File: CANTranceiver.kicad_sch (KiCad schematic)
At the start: 1 part, among them U3 IC TRANSCEIVER 1/1 8SO

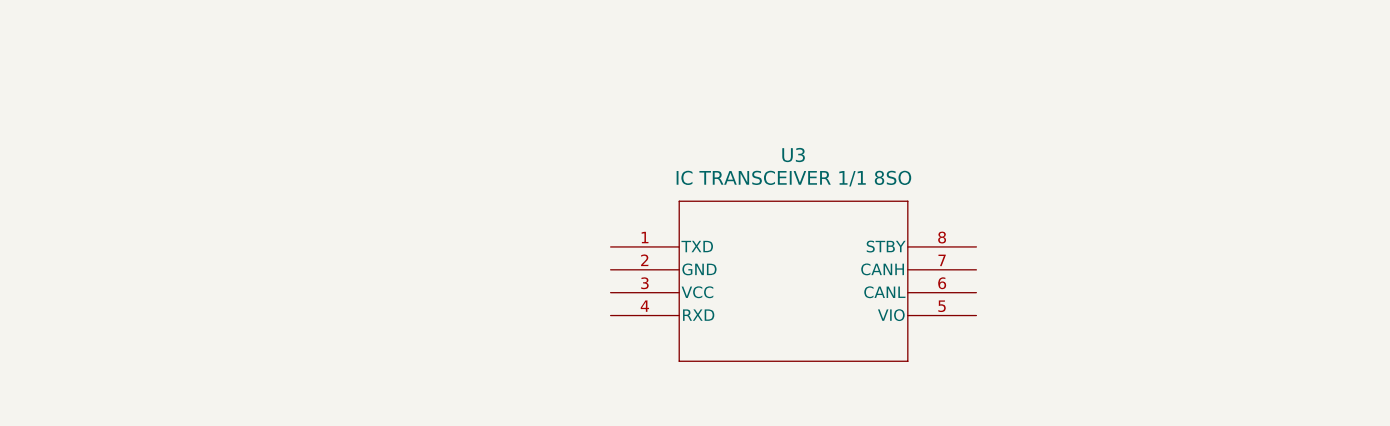
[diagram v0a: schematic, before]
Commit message: added stm pins
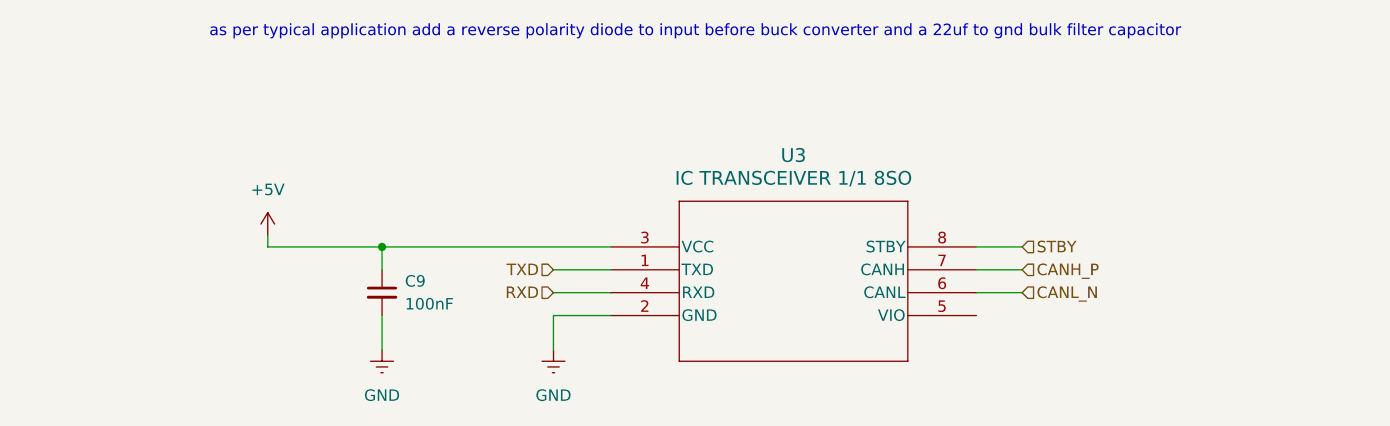
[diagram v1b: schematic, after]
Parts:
- added C9: 100nF, symbol Device:C_Small
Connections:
- net TXD: now reaches U3.1 (TXD)
- net GND: now reaches U3.2 (GND)
- net GND: now also C9.2
- net +5V: now reaches U3.3 (VCC)
- net +5V: now also C9.1
- net RXD: now reaches U3.4 (RXD)
- net CANL_N: now reaches U3.6 (CANL)
- net CANH_P: now reaches U3.7 (CANH)
- net STBY: now reaches U3.8 (STBY)
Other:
- note added: "as per typical application add a reverse polarity diode to input before buck converter and a 22uf to gnd bulk filter capacitor"

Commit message: finished can and power
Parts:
- added C11: 100nF, symbol Device:C_Small
- added C12: 22uF, symbol Device:C_Small_US
- added C13: 4.7nF, symbol Device:C_Small
- added D2: DIODE SCHOTTKY 30V 1A SOD323F, footprints:P39_SOD-323P, symbol symbols:SDB13HS-AQ
- added R10, R11: 60, symbol Device:R_Small_US
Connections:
- net CANH_P: now also R10.1, R11.2
- net GND: now also C11.2, C12.2, C13.2
- net 3V3: now reaches U3.5 (VIO)
- net 3V3: now also C11.1
- net +5V: no longer names the net of C9.1, U3.3 (VCC)
- net +5V: now also C12.1, D2.1 (K)
- net CANL_N renamed CANL_Filt
- new net: C13.1, R10.2, R11.1
- new net 5V: D2.2 (A)
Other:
- note added: "CANBus Split Termination"
- note removed: "as per typical application add a reverse polarity diode to input before buck converter and a 22uf to gnd bulk filter capacitor"
- moved on the sheet: C9, U3

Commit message: schematic done
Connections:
- net CANH_P: no longer R11.2
- net CANL_Filt renamed CANL_N
- net CANL_N: now also R11.2
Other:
- moved on the sheet: C11
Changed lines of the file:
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@@
-	)
-	(junction
-		(at 153.67 130.81)
-		(diameter 0)
-		(color 0 0 0 0)
 	)
 	(junction
@@
 	)
 	(junction
-		(at 153.67 97.79)
+		(at 106.68 60.96)
 		(diameter 0)
 		(color 0 0 0 0)
 	)
 	(junction
-		(at 106.68 60.96)
+		(at 195.58 68.58)
 		(diameter 0)
 		(color 0 0 0 0)
@@
 		(color 0 0 0 0)
 	)
-	(junction
-		(at 203.2 68.58)
-		(diameter 0)
-		(color 0 0 0 0)
-	)
-	(wire
-		(pts
-			(xy 203.2 76.2) (xy 203.2 78.74)
+	(wire
+		(pts
+			(xy 195.58 76.2) (xy 195.58 78.74)
 		)
 		(stroke
@@
 	(wire
 		(pts
+			(xy 195.58 68.58) (xy 195.58 71.12)
+		)
+		(stroke
+			(width 0)
+			(type default)
+		)
+	)
+	(wire
+		(pts
 			(xy 165.1 111.76) (xy 165.1 114.3)
 		)
@@
 	(wire
 		(pts
-			(xy 203.2 71.12) (xy 203.2 68.58)
-		)
-		(stroke
-			(width 0)
-			(type default)
-		)
-	)
-	(wire
-		(pts
-			(xy 203.2 68.58) (xy 172.72 68.58)
+			(xy 195.58 66.04) (xy 195.58 68.58)
 		)
 		(stroke
@@
 	(wire
 		(pts
-			(xy 172.72 63.5) (xy 186.69 63.5)
+			(xy 172.72 63.5) (xy 177.8 63.5)
 		)
 		(stroke
@@
 	(wire
 		(pts
-			(xy 153.67 130.81) (xy 162.56 130.81)
-		)
-		(stroke
-			(width 0)
-			(type default)
-		)
-	)
-	(wire
-		(pts
-			(xy 153.67 97.79) (xy 166.37 97.79)
-		)
-		(stroke
-			(width 0)
-			(type default)
-		)
-	)
-	(wire
-		(pts
 			(xy 172.72 60.96) (xy 177.8 60.96)
 		)
@@
 	(wire
 		(pts
-			(xy 203.2 66.04) (xy 203.2 68.58)
-		)
-		(stroke
-			(width 0)
-			(type default)
-		)
-	)
-	(wire
-		(pts
 			(xy 90.17 60.96) (xy 106.68 60.96)
 		)
@@
 	(wire
 		(pts
-			(xy 172.72 66.04) (xy 186.69 66.04)
+			(xy 172.72 66.04) (xy 177.8 66.04)
 		)
 		(stroke
@@
 	(wire
 		(pts
+			(xy 172.72 68.58) (xy 195.58 68.58)
+		)
+		(stroke
+			(width 0)
+			(type default)
+		)
+	)
+	(wire
+		(pts
 			(xy 153.67 121.92) (xy 153.67 130.81)
 		)
@@
 			(width 0)
 			(type default)
-		)
-	)
-	(label "CANH_Filt"
-		(at 143.51 130.81 180)
-		(effects
-			(font
-				(size 1.27 1.27)
-			)
-			(justify right bottom)
-		)
-	)
-	(label "CANH_Filt"
-		(at 143.51 97.79 180)
-		(effects
-			(font
-				(size 1.27 1.27)
-			)
-			(justify right bottom)
-		)
-	)
-	(label "CANL_Filt"
-		(at 186.69 66.04 0)
-		(effects
-			(font
-				(size 1.27 1.27)
-			)
-			(justify left bottom)
-		)
-	)
-	(label "CANH_Filt"
-		(at 186.69 63.5 0)
-		(effects
-			(font
-				(size 1.27 1.27)
-			)
-			(justify left bottom)
 		)
 	)
@@
 		)
 	)
+	(hierarchical_label "CANH_P"
+		(shape input)
+		(at 143.51 97.79 180)
+		(effects
+			(font
+				(size 1.27 1.27)
+			)
+			(justify right)
+		)
+	)
 	(hierarchical_label "CANL_N"
 		(shape input)
-		(at 162.56 130.81 0)
+		(at 177.8 66.04 0)
+		(effects
+			(font
+				(size 1.27 1.27)
+			)
+			(justify left)
+		)
+	)
+	(hierarchical_label "CANH_P"
+		(shape input)
+		(at 177.8 63.5 0)
 		(effects
 			(font
@@
 		)
 	)
-	(hierarchical_label "CANH_P"
+	(hierarchical_label "CANL_N"
 		(shape input)
-		(at 166.37 97.79 0)
+		(at 143.51 130.81 180)
 		(effects
 			(font
 				(size 1.27 1.27)
 			)
-			(justify left)
+			(justify right)
 		)
 	)
@@
 	(symbol
 		(lib_id "power:GNDREF")
-		(at 203.2 78.74 0)
+		(at 195.58 78.74 0)
 		(unit 1)
 		(body_style 1)
@@
 		(fields_autoplaced yes)
 		(property "Reference" "#PWR026"
-			(at 203.2 85.09 0)
+			(at 195.58 85.09 0)
 			(hide yes)
 			(show_name no)
@@
 		)
 		(property "Value" "GND"
-			(at 203.2 83.82 0)
+			(at 195.58 83.82 0)
 			(show_name no)
 			(do_not_autoplace no)
@@
 		)
 		(property "Footprint" ""
-			(at 203.2 78.74 0)
+			(at 195.58 78.74 0)
 			(hide yes)
 			(show_name no)
@@
 		)
 		(property "Datasheet" ""
-			(at 203.2 78.74 0)
+			(at 195.58 78.74 0)
 			(hide yes)
 			(show_name no)
@@
 		)
 		(property "Description" "Power symbol creates a global label with name \"GNDREF\" , reference supply ground"
-			(at 203.2 78.74 0)
+			(at 195.58 78.74 0)
 			(hide yes)
 			(show_name no)
@@
 	(symbol
 		(lib_id "Device:C_Small")
-		(at 203.2 73.66 0)
+		(at 195.58 73.66 0)
 		(unit 1)
 		(body_style 1)
@@
 		(fields_autoplaced yes)
 		(property "Reference" "C11"
-			(at 205.74 72.3962 0)
+			(at 198.12 72.3962 0)
 			(show_name no)
 			(do_not_autoplace no)
@@
 		)
 		(property "Value" "100nF"
-			(at 205.74 74.9362 0)
+			(at 198.12 74.9362 0)
 			(show_name no)
 			(do_not_autoplace no)
@@
 		)
 		(property "Footprint" ""
-			(at 203.2 73.66 0)
+			(at 195.58 73.66 0)
 			(hide yes)
 			(show_name no)
@@
 		)
 		(property "Datasheet" ""
-			(at 203.2 73.66 0)
+			(at 195.58 73.66 0)
 			(hide yes)
 			(show_name no)
@@
 		)
 		(property "Description" "Unpolarized capacitor, small symbol"
-			(at 203.2 73.66 0)
+			(at 195.58 73.66 0)
 			(hide yes)
 			(show_name no)
@@
 	(symbol
 		(lib_id "power:+5V")
-		(at 203.2 66.04 0)
+		(at 195.58 66.04 0)
 		(unit 1)
 		(body_style 1)
@@
 		(fields_autoplaced yes)
 		(property "Reference" "#PWR027"
-			(at 203.2 69.85 0)
+			(at 195.58 69.85 0)
 			(hide yes)
 			(show_name no)
@@
 		)
 		(property "Value" "3V3"
-			(at 203.2 60.96 0)
+			(at 195.58 60.96 0)
 			(show_name no)
 			(do_not_autoplace no)
@@
 		)
 		(property "Footprint" ""
-			(at 203.2 66.04 0)
+			(at 195.58 66.04 0)
 			(hide yes)
 			(show_name no)
@@
 		)
 		(property "Datasheet" ""
-			(at 203.2 66.04 0)
+			(at 195.58 66.04 0)
 			(hide yes)
 			(show_name no)
@@
 		)
 		(property "Description" "Power symbol creates a global label with name \"+5V\""
-			(at 203.2 66.04 0)
-			(hide yes)
-			(show_name no)
+			(at 195.58 66.04 0)
+			(hide yes)
+			(show_name no)

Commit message: damir review
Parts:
- removed D2: DIODE SCHOTTKY 30V 1A SOD323F, footprints:P39_SOD-323P, symbol symbols:SDB13HS-AQ
- added D1, D2: TVS DIODE 36VWM 76.8VC SOT233, footprints:P200_SOT-23, symbol symbols:Diode-NC_pin
- R10, R11: value 60 -> 60.4
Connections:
- net 5V: now also C12.1, C9.1, U3.3 (VCC)
- net CANH_P: now also D1.2 (C)
- net CANL_N: now also D2.2 (C)
- net GND: now also D1.1 (A), D2.1 (A)
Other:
- note added: "C = 1/2piRf = 5.3nF -> 4.7nF f = 500kHz R = 60.4"

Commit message: tweaked a little
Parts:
- removed D1, D2: TVS DIODE 36VWM 76.8VC SOT233, footprints:P200_SOT-23, symbol symbols:Diode-NC_pin
- added D4, D5: TVS DIODE 5VWM 12.5VC SOD-523, footprints:P38_SOD-523, symbol symbols:Diode
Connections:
- net CANH_P: now also D4.2 (C)
- net CANL_N: now also D5.2 (C)
- net GND: now also D4.1 (A), D5.1 (A)
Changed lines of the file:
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@@
+	)
+	(symbol
+		(lib_id "symbols:Diode")
+		(at 137.16 104.14 90)
+		(unit 1)
+		(body_style 1)
+		(exclude_from_sim no)
+		(in_bom yes)
+		(on_board yes)
+		(in_pos_files yes)
+		(dnp no)
+		(property "Reference" "D4"
+			(at 130.302 102.87 90)
+			(show_name no)
+			(do_not_autoplace no)
+			(effects
+				(font
+					(size 1.27 1.27)
+				)
+				(justify right)
+			)
+		)
+		(property "Value" "TVS DIODE 5VWM 12.5VC SOD-523"
+			(at 99.314 105.156 90)
+			(show_name no)
+			(do_not_autoplace no)
+			(effects
+				(font
+					(size 1.27 1.27)
+				)
+				(justify right)
+			)
+		)
+		(property "Footprint" "footprints:P38_SOD-523"
+			(at 135.89 104.14 90)
+			(hide yes)
+			(show_name no)
+			(do_not_autoplace no)
+			(effects
+				(font
+					(size 1.27 1.27)
+				)
+			)
+		)
+		(property "Datasheet" "https://www.digikey.ca/en/products/detail/diotec-semiconductor/ESD5B5V0WT/22189401"
+			(at 139.7 104.14 0)
+			(hide yes)
+			(show_name no)
+			(do_not_autoplace no)
+			(effects
+				(font
+					(size 1.27 1.27)
+				)
+			)
+		)
+		(property "Description" "12.5V Clamp 4A (8/20µs) Ipp Tvs Diode Surface Mount SOD-523"
+			(at 137.16 104.14 0)
+			(hide yes)
+			(show_name no)
+			(do_not_autoplace no)
+			(effects
+				(font
+					(size 1.27 1.27)
+				)
+			)
+		)
+		(pin "2"
+		)
+		(pin "1"
+		)
+		(instances
+			(project "bms-main"
+				(path "/d7e1c873-142c-4805-8303-47f5b9830fe8/3499863e-1965-40fb-acb8-8c0f2bec52b8"
+					(reference "D4")
+					(unit 1)
+				)
+			)
+		)
 	)
 	(symbol
@@
 	)
 	(symbol
-		(lib_id "symbols:Diode-NC_pin")
-		(at 140.97 137.16 90)
-		(unit 1)
-		(body_style 1)
-		(exclude_from_sim no)
-		(in_bom yes)
-		(on_board yes)
-		(in_pos_files yes)
-		(dnp no)
-		(fields_autoplaced yes)
-		(property "Reference" "D2"
-			(at 144.78 135.9534 90)
-			(show_name no)
-			(do_not_autoplace no)
-			(effects
-				(font
-					(size 1.27 1.27)
-				)
-				(justify right)
-			)
-		)
-		(property "Value" "TVS DIODE 36VWM 76.8VC SOT233"
-			(at 144.78 138.4934 90)
-			(show_name no)
-			(do_not_autoplace no)
-			(effects
-				(font
-					(size 1.27 1.27)
-				)
-				(justify right)
-			)
-		)
-		(property "Footprint" "footprints:P200_SOT-23"
-			(at 137.16 138.43 90)
-			(hide yes)
-			(show_name no)
-			(do_not_autoplace no)
-			(effects
-				(font
-					(size 1.27 1.27)
-				)
-			)
-		)
-		(property "Datasheet" "https://www.digikey.ca/en/products/detail/diotec-semiconductor/PSOT36C/22191308"
-			(at 146.05 137.16 0)
-			(hide yes)
-			(show_name no)
-			(do_not_autoplace no)
-			(effects
-				(font
-					(size 1.27 1.27)
-				)
-			)
-		)
-		(property "Description" "76.8V Clamp 9A (8/20µs) Ipp Tvs Diode Surface Mount SOT-23-3 (TO-236)"
-			(at 140.97 137.16 0)
-			(hide yes)
-			(show_name no)
-			(do_not_autoplace no)
-			(effects
-				(font
-					(size 1.27 1.27)
-				)
-			)
-		)
-		(pin "1"
-		)
-		(pin "3"
-		)
-		(pin "2"
-		)
-		(instances
-			(project "bms-main"
-				(path "/d7e1c873-142c-4805-8303-47f5b9830fe8/3499863e-1965-40fb-acb8-8c0f2bec52b8"
-					(reference "D2")
-					(unit 1)
-				)
-			)
-		)
-	)
-	(symbol
 		(lib_id "power:GNDREF")
 		(at 90.17 73.66 0)
@@
 	)
 	(symbol
-		(lib_id "symbols:Diode-NC_pin")
-		(at 139.7 102.87 90)
-		(unit 1)
-		(body_style 1)
-		(exclude_from_sim no)
-		(in_bom yes)
-		(on_board yes)
-		(in_pos_files yes)
-		(dnp no)
-		(property "Reference" "D1"
-			(at 100.584 102.616 90)
-			(show_name no)
-			(do_not_autoplace no)
-			(effects
-				(font
-					(size 1.27 1.27)
-				)
-				(justify right)
-			)
-		)
-		(property "Value" "TVS DIODE 36VWM 76.8VC SOT233"
-			(at 100.584 105.156 90)
-			(show_name no)
-			(do_not_autoplace no)
-			(effects
-				(font
-					(size 1.27 1.27)
-				)
-				(justify right)
-			)
-		)
-		(property "Footprint" "footprints:P200_SOT-23"
-			(at 135.89 104.14 90)
-			(hide yes)
-			(show_name no)
-			(do_not_autoplace no)
-			(effects
-				(font
-					(size 1.27 1.27)
-				)
-			)
-		)
-		(property "Datasheet" "https://www.digikey.ca/en/products/detail/diotec-semiconductor/PSOT36C/22191308"
-			(at 144.78 102.87 0)
-			(hide yes)
-			(show_name no)
-			(do_not_autoplace no)
-			(effects
-				(font
-					(size 1.27 1.27)
-				)
-			)
-		)
-		(property "Description" "76.8V Clamp 9A (8/20µs) Ipp Tvs Diode Surface Mount SOT-23-3 (TO-236)"
-			(at 139.7 102.87 0)
-			(hide yes)
-			(show_name no)
-			(do_not_autoplace no)
-			(effects
-				(font
-					(size 1.27 1.27)
-				)
-			)
-		)
-		(pin "1"
-		)
-		(pin "3"
-		)
-		(pin "2"
-		)
-		(instances
-			(project "bms-main"
-				(path "/d7e1c873-142c-4805-8303-47f5b9830fe8/3499863e-1965-40fb-acb8-8c0f2bec52b8"
-					(reference "D1")
-					(unit 1)
-				)
-			)
-		)
-	)
-	(symbol
 		(lib_id "Device:R_Small_US")
 		(at 153.67 106.68 0)
@@
 					(unit 1)
 				)
+			)
+		)
+	)
+	(symbol
+		(lib_id "symbols:Diode")
+		(at 138.43 138.43 90)
+		(unit 1)
+		(body_style 1)
+		(exclude_from_sim no)
+		(in_bom yes)
+		(on_board yes)
+		(in_pos_files yes)
+		(dnp no)
+		(fields_autoplaced yes)
+		(property "Reference" "D5"
+			(at 140.97 137.1599 90)
+			(show_name no)
+			(do_not_autoplace no)
+			(effects
+				(font
+					(size 1.27 1.27)
+				)
+				(justify right)
+			)
+		)
+		(property "Value" "TVS DIODE 5VWM 12.5VC SOD-523"
+			(at 140.97 139.6999 90)
+			(show_name no)
+			(do_not_autoplace no)
+			(effects
+				(font
+					(size 1.27 1.27)
+				)
+				(justify right)
+			)
+		)
+		(property "Footprint" "footprints:P38_SOD-523"
+			(at 137.16 138.43 90)
+			(hide yes)
+			(show_name no)
+			(do_not_autoplace no)
+			(effects
+				(font
+					(size 1.27 1.27)
+				)
+			)
+		)
+		(property "Datasheet" "https://www.digikey.ca/en/products/detail/diotec-semiconductor/ESD5B5V0WT/22189401"
+			(at 140.97 138.43 0)
+			(hide yes)
+			(show_name no)
+			(do_not_autoplace no)
+			(effects
+				(font
+					(size 1.27 1.27)
+				)
+			)
+		)
+		(property "Description" "12.5V Clamp 4A (8/20µs) Ipp Tvs Diode Surface Mount SOD-523"
+			(at 138.43 138.43 0)
+			(hide yes)
+			(show_name no)
+			(do_not_autoplace no)
+			(effects
+				(font
+					(size 1.27 1.27)
+				)
+			)
+		)
+		(pin "2"
+		)
+		(pin "1"
+		)
+		(instances
+			(project "bms-main"
+				(path "/d7e1c873-142c-4805-8303-47f5b9830fe8/3499863e-1965-40fb-acb8-8c0f2bec52b8"
+					(reference "D5")
+					(unit 1)
+				)

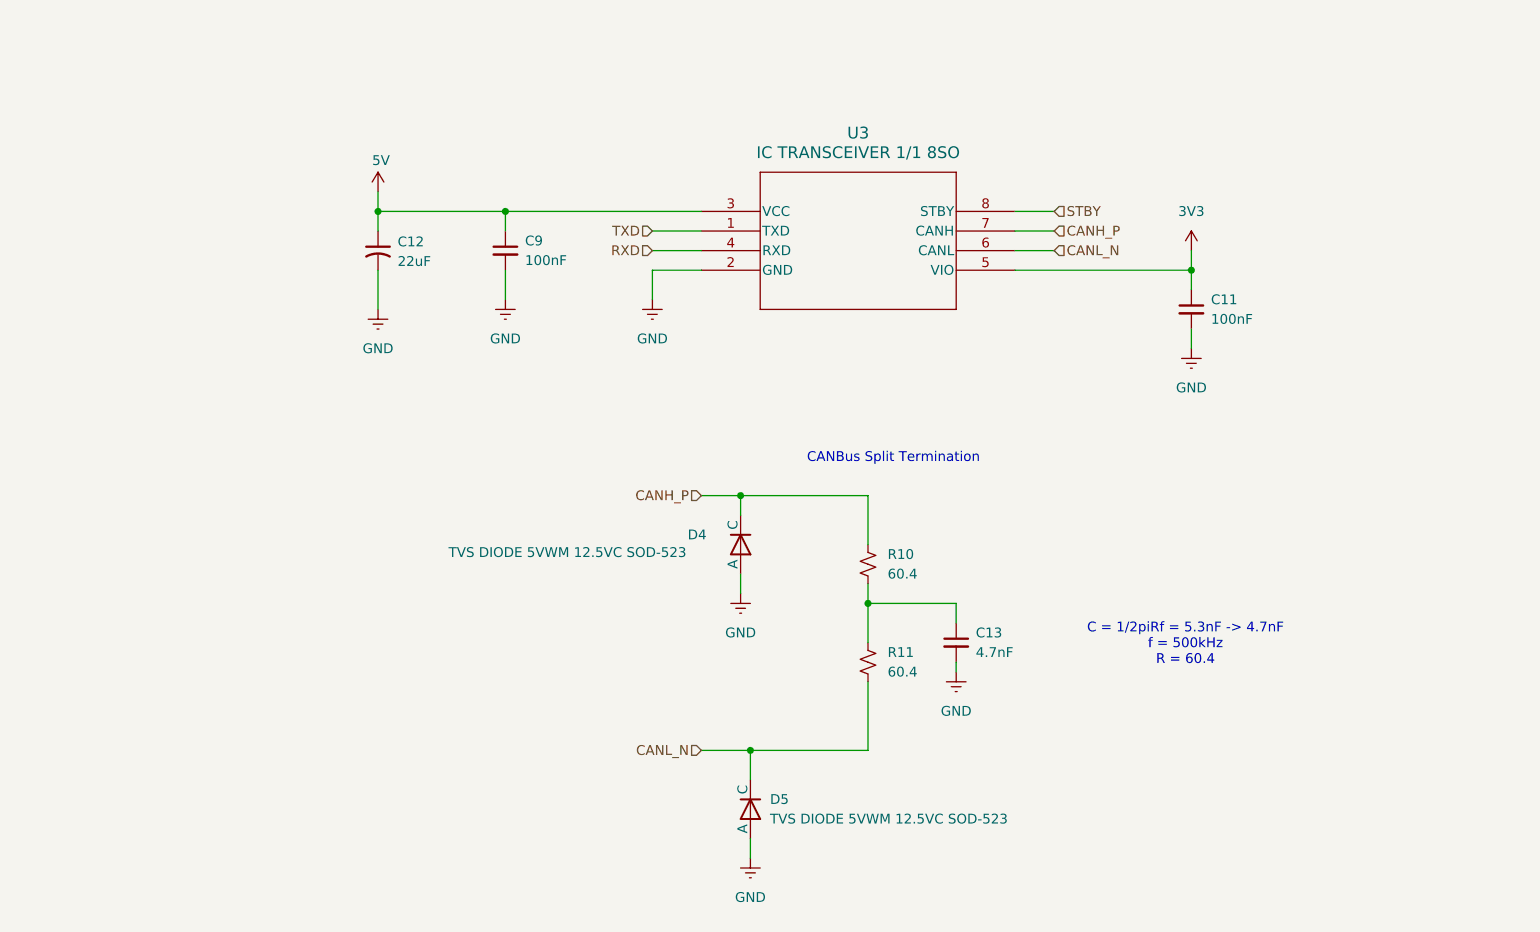
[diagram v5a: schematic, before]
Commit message: added passives
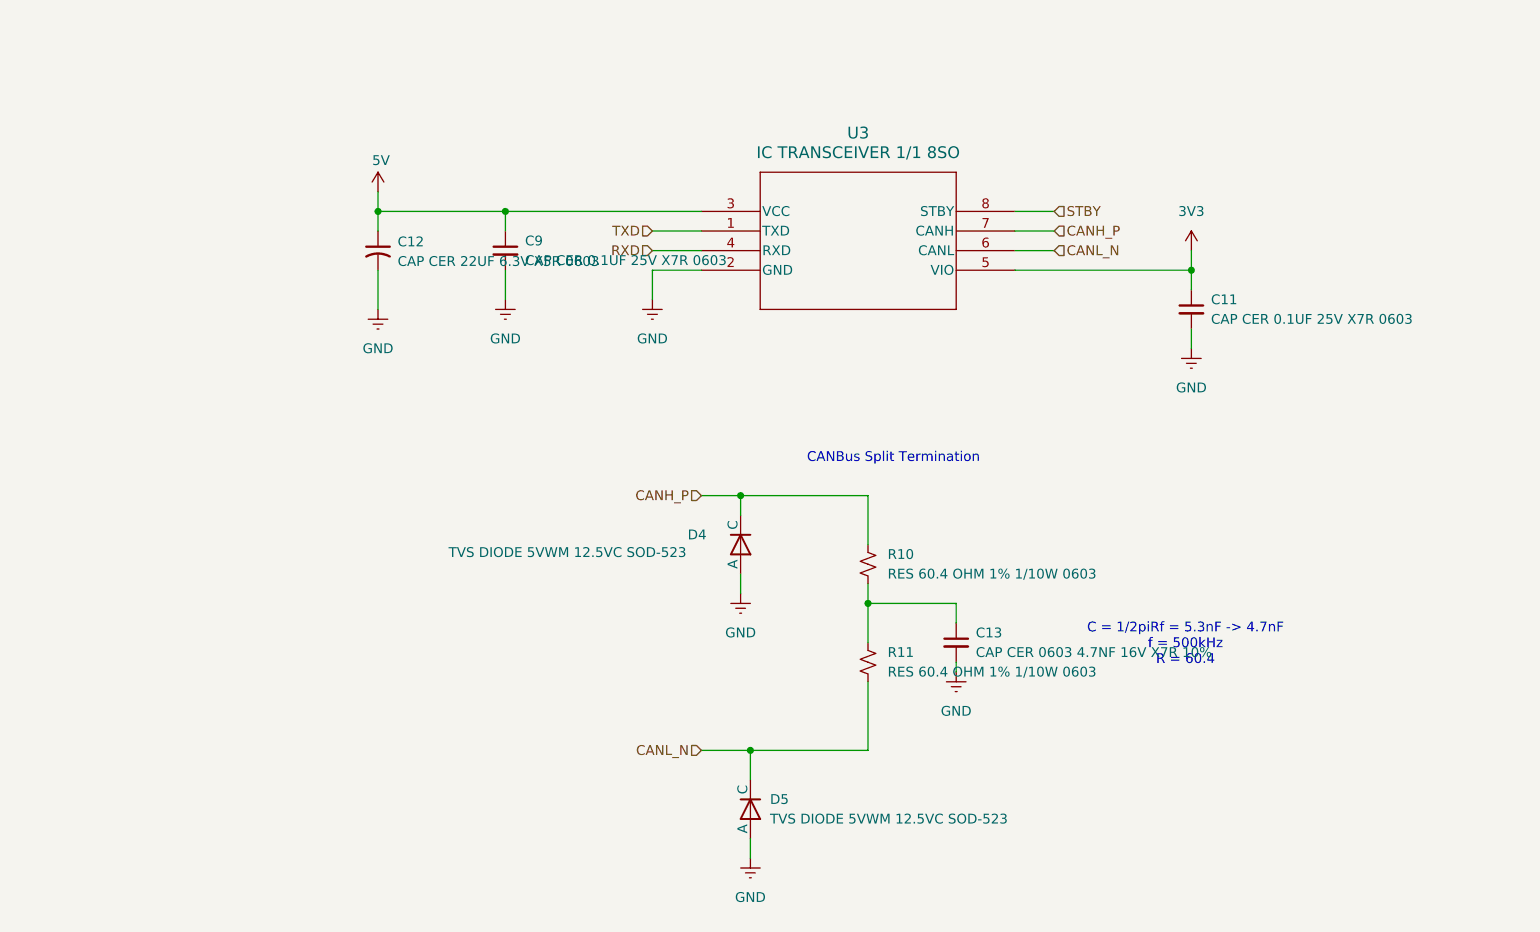
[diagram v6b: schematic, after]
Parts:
- C11, C9: value 100nF -> CAP CER 0.1UF 25V X7R 0603; footprint (none) -> Capacitor_SMD:C_0603_1608Metric
- C12: value 22uF -> CAP CER 22UF 6.3V X5R 0603; footprint (none) -> Capacitor_SMD:C_0603_1608Metric
- C13: value 4.7nF -> CAP CER 0603 4.7NF 16V X7R 10%; footprint (none) -> Capacitor_SMD:C_0603_1608Metric
- R10, R11: value 60.4 -> RES 60.4 OHM 1% 1/10W 0603; footprint (none) -> Resistor_SMD:R_0603_1608Metric
